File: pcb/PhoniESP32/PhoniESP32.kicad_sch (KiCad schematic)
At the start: 13 parts, among them J3 Conn_Buttons, U3 ESP32-C6-MINI-1-N4

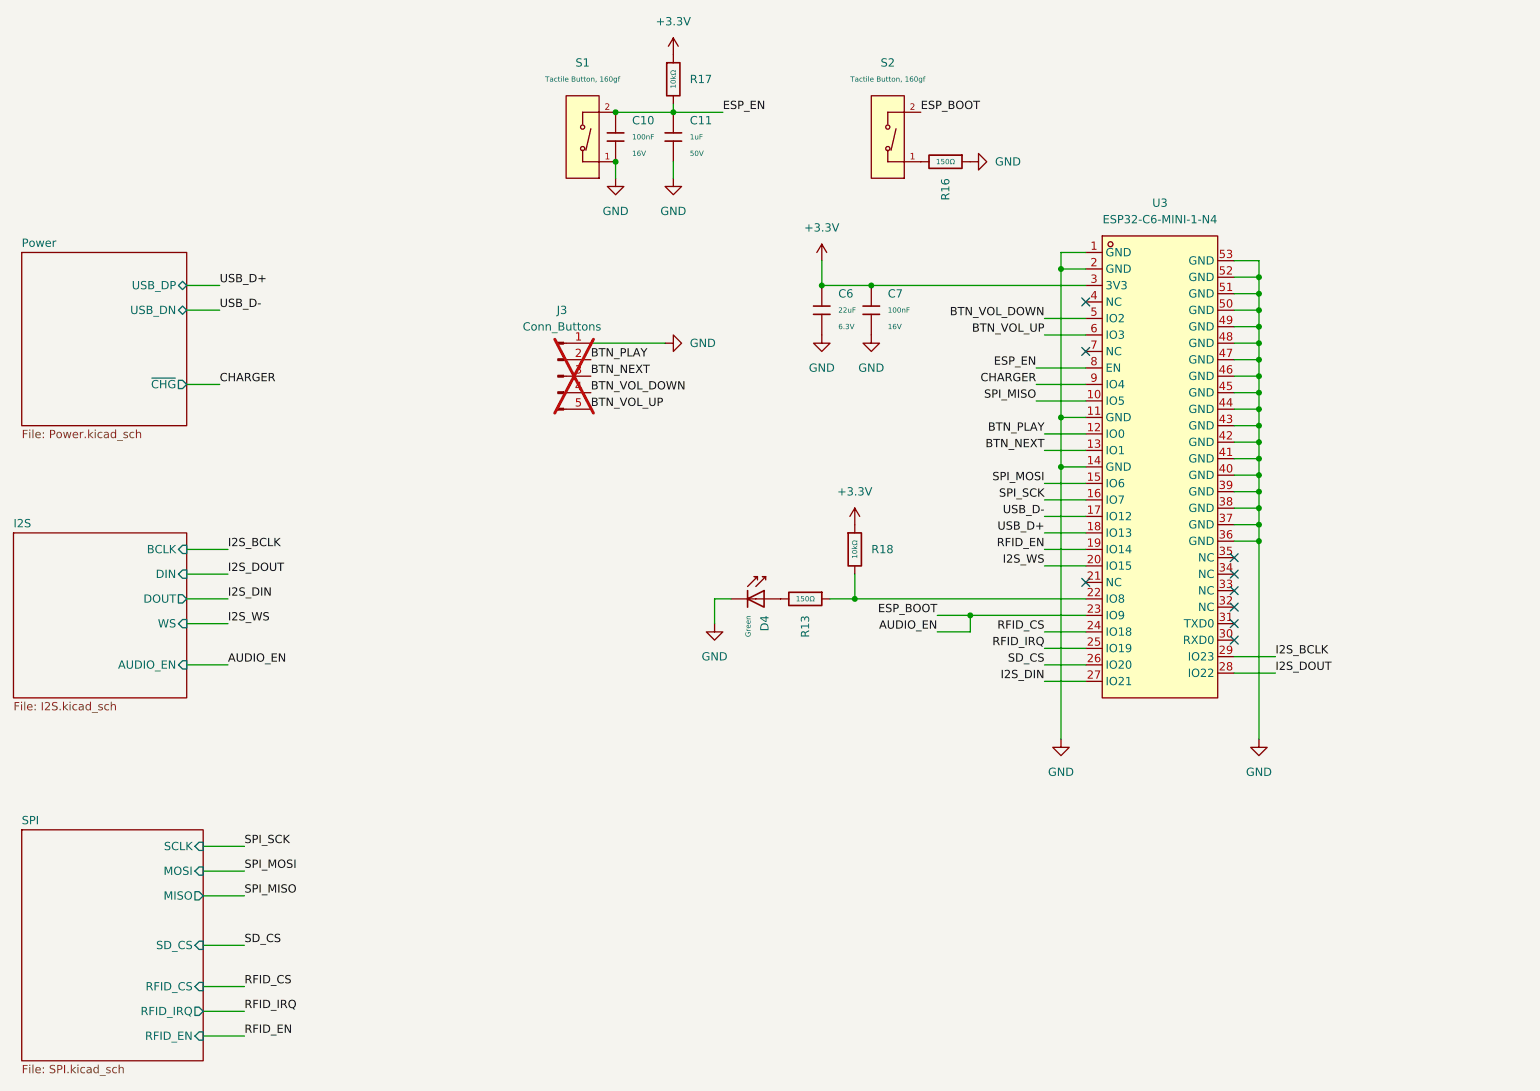
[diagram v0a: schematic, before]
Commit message: fix(pcb): add 22 Ohm resistors on USB data lines
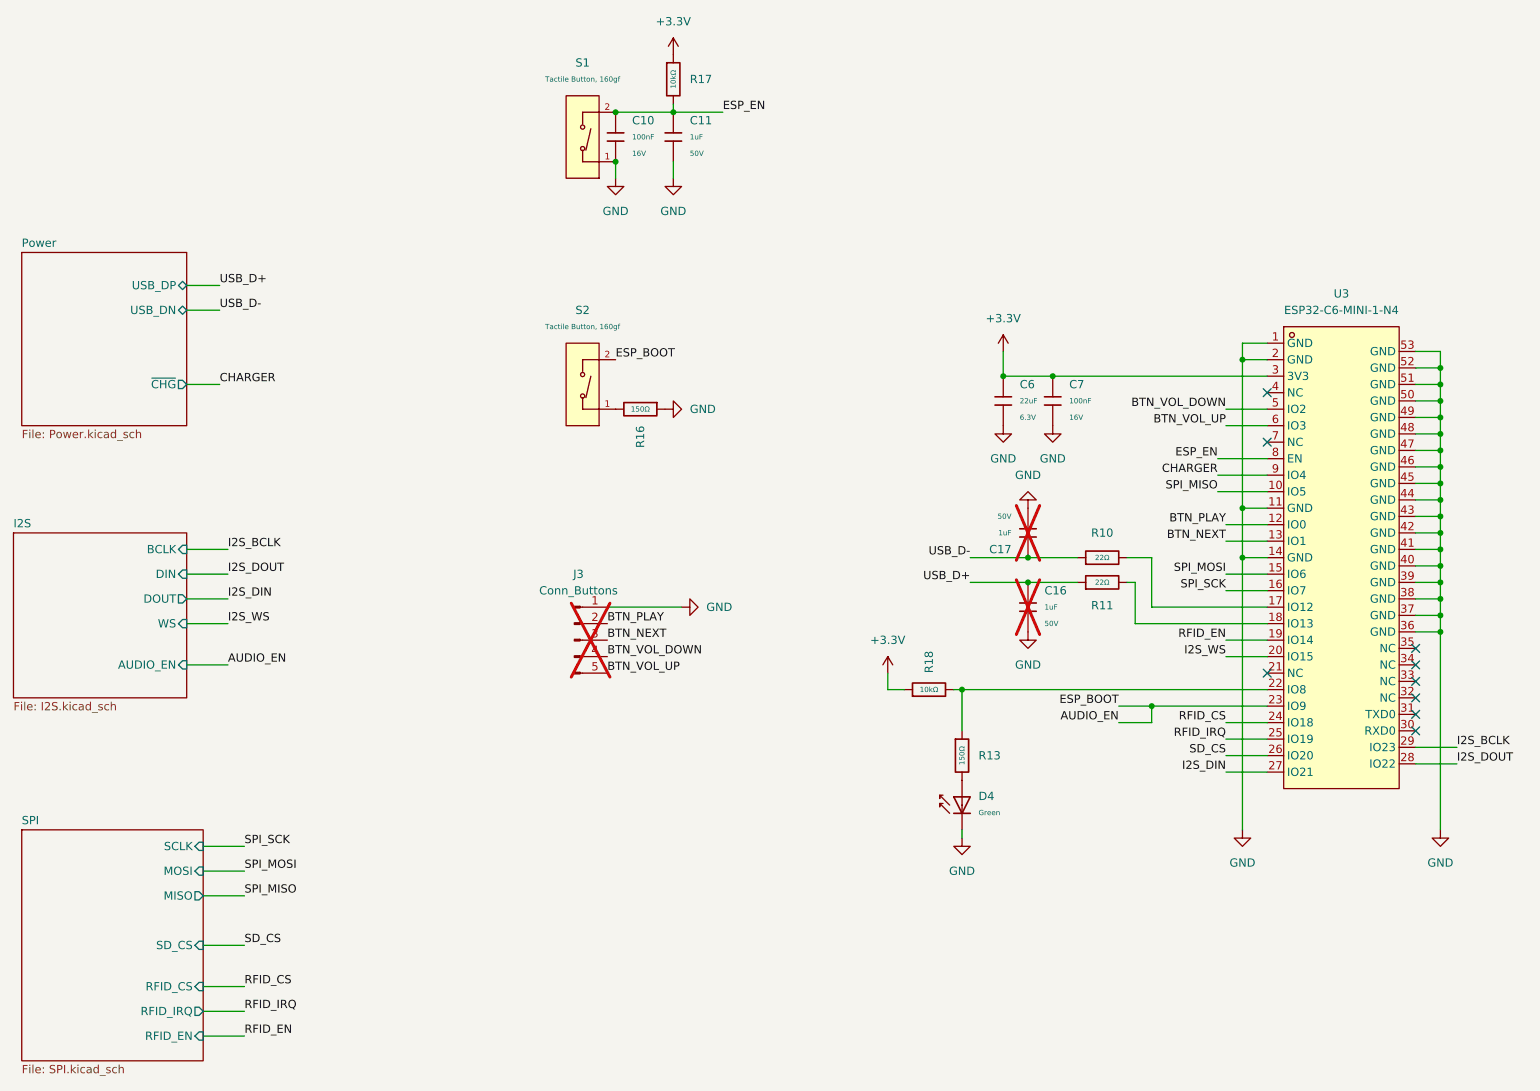
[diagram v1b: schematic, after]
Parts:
- added C16, C17: 1uF, PCM_JLCPCB:C_0603, symbol PCM_JLCPCB-Capacitors:0603,1uF
- added R10, R11: 22Ω, PCM_JLCPCB:R_0603, symbol PCM_JLCPCB-Resistors:0603,22Ω
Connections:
- net GND: now also C16.2, C17.2
- net USB_D+: now also C16.1, R11.1; no longer U3.18 (IO13)
- net USB_D-: now also C17.1, R10.1; no longer U3.17 (IO12)
- new net: R10.2, U3.17 (IO12)
- new net: R11.2, U3.18 (IO13)
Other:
- moved on the sheet: C6, C7, D4, J3, R13, R16, R18, S2, U3

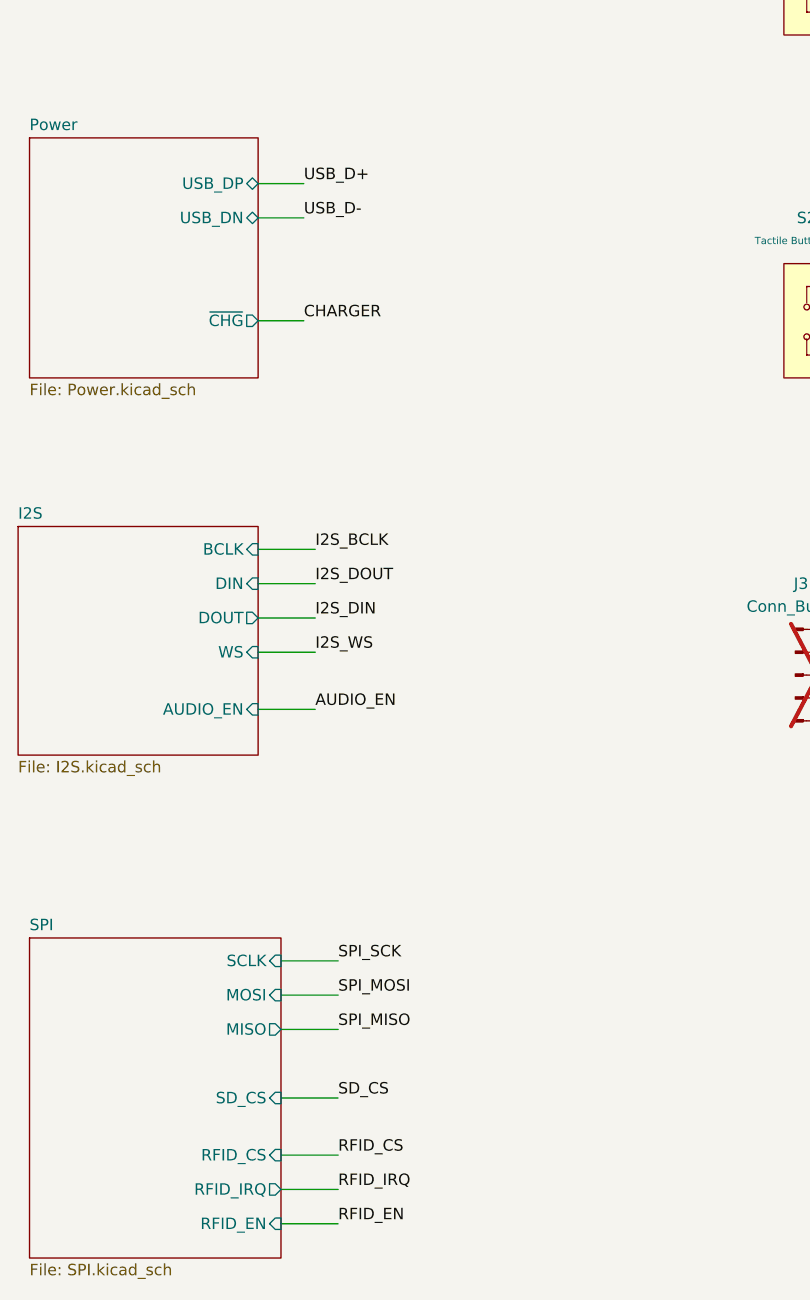
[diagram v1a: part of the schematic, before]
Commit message: feat(pcb): place test points and placeholders
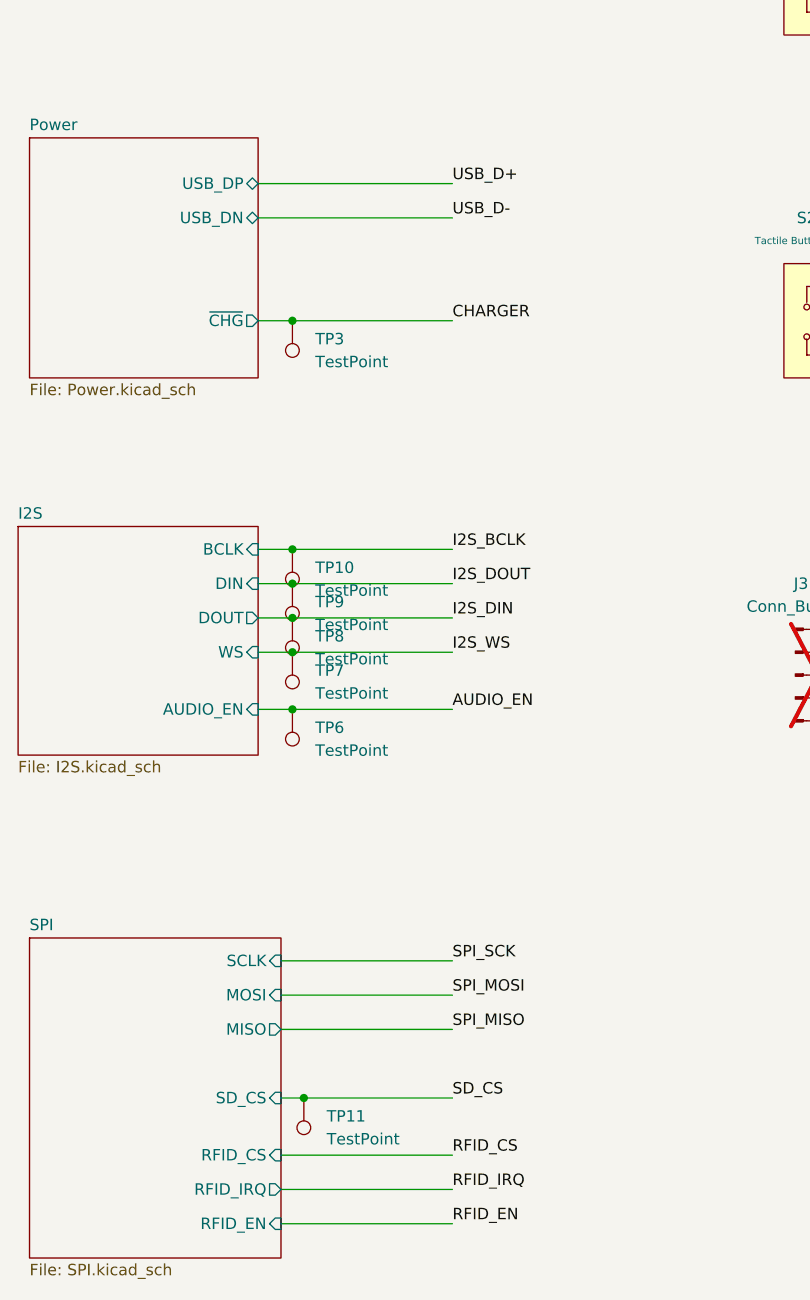
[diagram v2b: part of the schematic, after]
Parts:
- added TP10, TP11, TP3, TP6, TP7, TP8, TP9: TestPoint, TestPoint:TestPoint_Pad_D1.0mm, symbol Connector:TestPoint
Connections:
- net AUDIO_EN: now also TP6.1
- net CHARGER: now also TP3.1
- net I2S_BCLK: now also TP10.1
- net I2S_DIN: now also TP8.1
- net I2S_DOUT: now also TP9.1
- net I2S_WS: now also TP7.1
- net SD_CS: now also TP11.1

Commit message: feat(pcb): initial traces
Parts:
- removed R10, R11: 22Ω, PCM_JLCPCB:R_0603, symbol PCM_JLCPCB-Resistors:0603,22Ω
- added R10, R11: 22Ω, PCM_JLCPCB:R_0402, symbol PCM_JLCPCB-Resistors:0402,22Ω
- U3: footprint JLCPCB:WIFIM-SMD_61P-L16.6-W13.2-P0.80-ESP32-C6-MINI-1-N4 -> RF_Module:ESP32-C6-MINI-1
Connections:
- net USB_D+: now also R11.1
- net USB_D-: now also R10.1
- net at U3.17 (IO12): now also R10.2
- net at U3.18 (IO13): now also R11.2

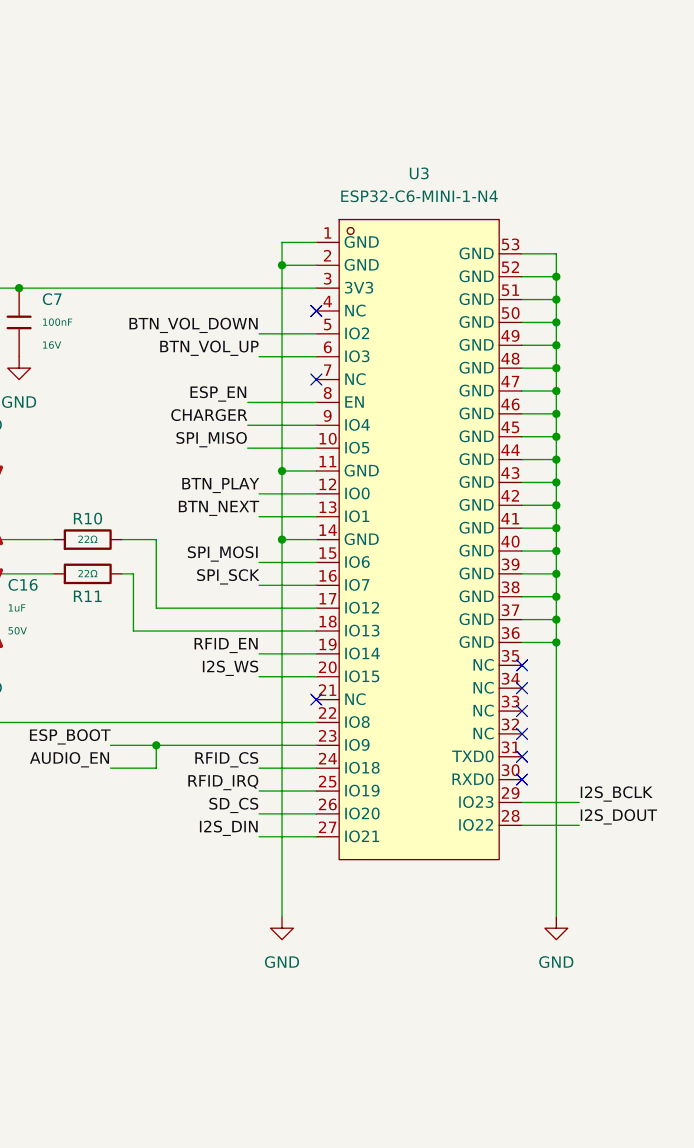
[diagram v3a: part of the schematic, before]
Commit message: chore(pcb): switch from PCB antenna to connector
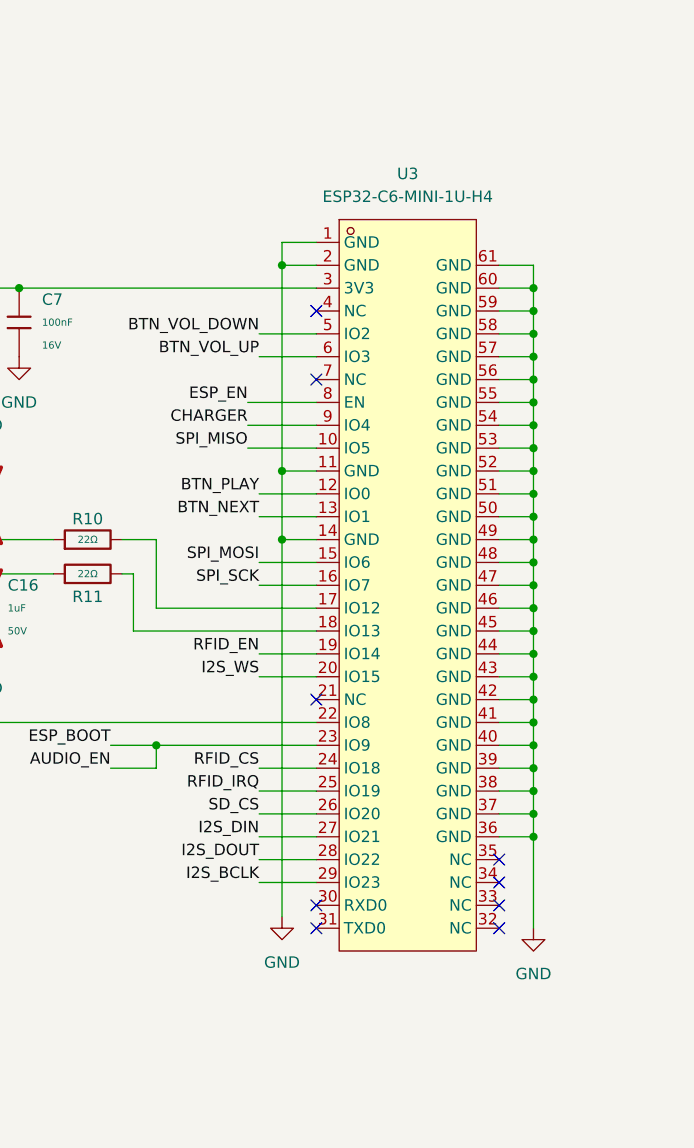
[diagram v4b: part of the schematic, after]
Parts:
- removed U3: ESP32-C6-MINI-1-N4, RF_Module:ESP32-C6-MINI-1, symbol JLCPCB:ESP32-C6-MINI-1-N4
- added U3: ESP32-C6-MINI-1U-H4, JLCPCB:WIFIM-SMD_61P-L13.2-W12.5-P0.80, symbol JLCPCB:ESP32-C6-MINI-1U-H4
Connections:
- net +3.3V: now also U3.3 (3V3)
- net AUDIO_EN: now also U3.23 (IO9)
- net BTN_NEXT: now also U3.13 (IO1)
- net BTN_PLAY: now also U3.12 (IO0)
- net BTN_VOL_DOWN: now also U3.5 (IO2)
- net BTN_VOL_UP: now also U3.6 (IO3)
- net CHARGER: now also U3.9 (IO4)
- net ESP_EN: now also U3.8 (EN)
- net GND: now also U3.1 (GND), U3.11 (GND), U3.14 (GND), U3.2 (GND), U3.36 (GND), U3.37 (GND), U3.38 (GND), U3.39 (GND), U3.40 (GND), U3.41 (GND), U3.42 (GND), U3.43 (GND), U3.44 (GND), U3.45 (GND), U3.46 (GND), U3.47 (GND), U3.48 (GND), U3.49 (GND), U3.50 (GND), U3.51 (GND), U3.52 (GND), U3.53 (GND), U3.54 (GND), U3.55 (GND), U3.56 (GND), U3.57 (GND), U3.58 (GND), U3.59 (GND), U3.60 (GND), U3.61 (GND)
- net I2S_BCLK: now also U3.29 (IO23)
- net I2S_DIN: now also U3.27 (IO21)
- net I2S_DOUT: now also U3.28 (IO22)
- net I2S_WS: now also U3.20 (IO15)
- net RFID_CS: now also U3.24 (IO18)
- net RFID_EN: now also U3.19 (IO14)
- net RFID_IRQ: now also U3.25 (IO19)
- net SD_CS: now also U3.26 (IO20)
- net SPI_MISO: now also U3.10 (IO5)
- net SPI_MOSI: now also U3.15 (IO6)
- net SPI_SCK: now also U3.16 (IO7)
- net at R10.2: now also U3.17 (IO12)
- net at R11.2: now also U3.18 (IO13)
- net at R13.1, R18.2: now also U3.22 (IO8)
